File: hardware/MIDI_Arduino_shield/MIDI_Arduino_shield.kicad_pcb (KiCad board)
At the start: 2 copper layers, 54.6 x 69.8 mm, 31 parts, among them J2 MIDI OUT, J3 MIDI IN, J4 I2C, Q1 2N3906, SW1 RotaryEncoder_Switch, SW2 SW_Push, SW3 SW_Push, SW4 SW_DPDT_x2, U2 6N139

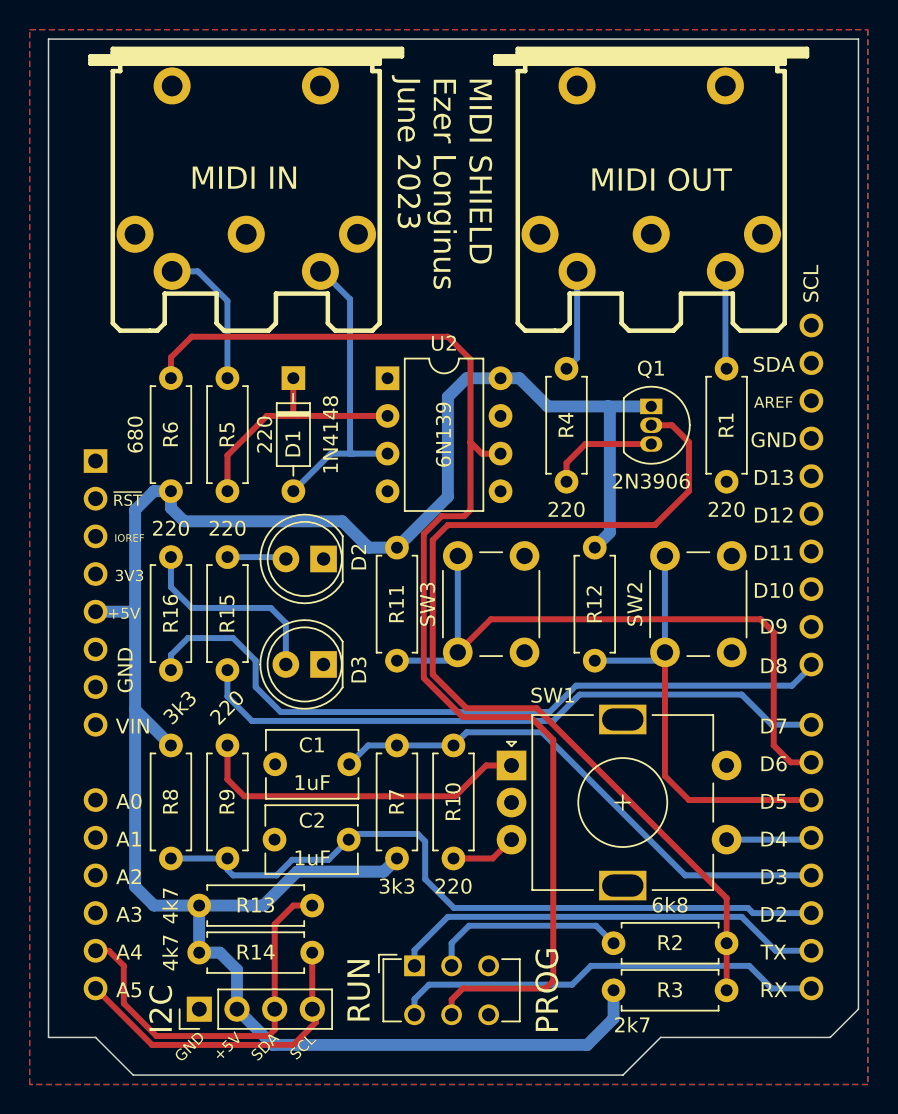
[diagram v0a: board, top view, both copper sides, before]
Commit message: MIDI Breakout Variations
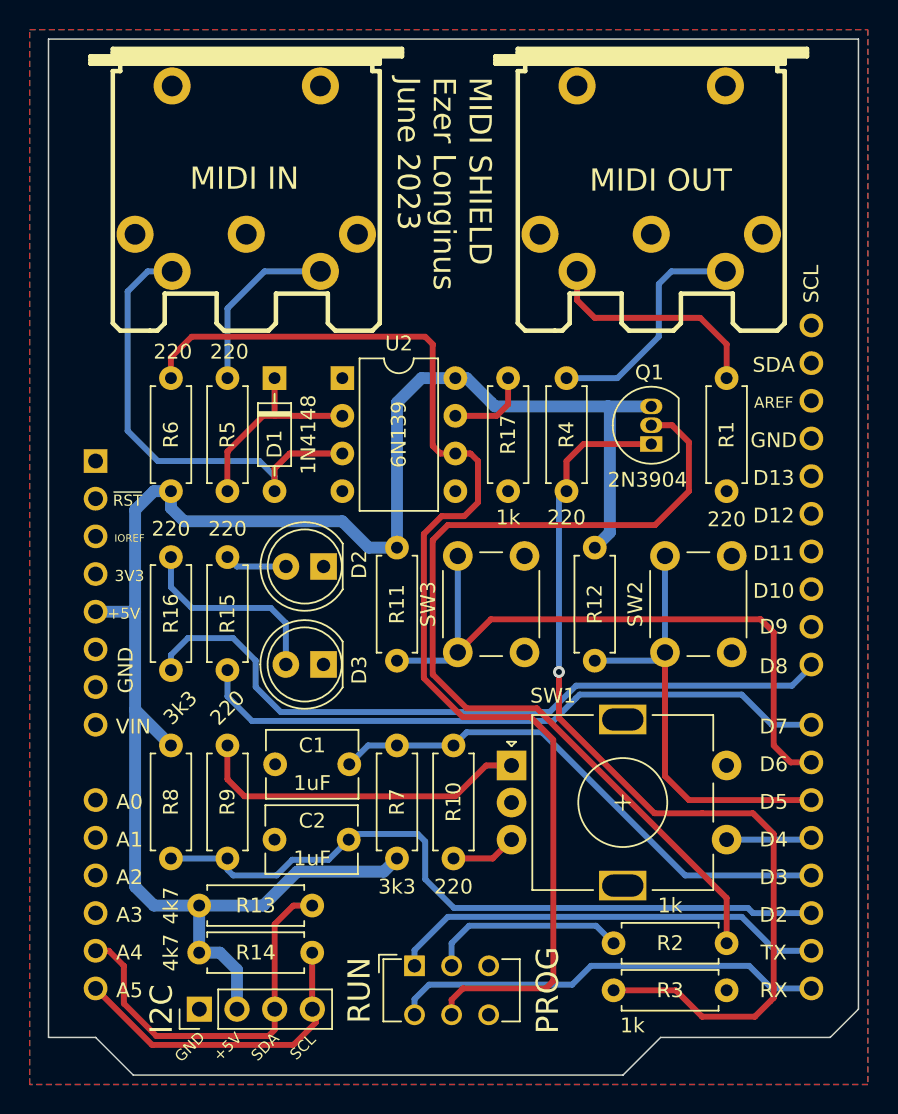
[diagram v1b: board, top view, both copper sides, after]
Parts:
- added R17: 1k, Resistor_THT:R_Axial_DIN0207_L6.3mm_D2.5mm_P7.62mm_Horizontal, F.Cu at (152.9, 78.7)
- Q1: value 2N3906 -> 2N3904
- R2: value 6k8 -> 1k
- R3: value 2k7 -> 1k
- R6: value 680 -> 220
- moved U2 3.05 mm to (141.7, 78.7)
- moved Q1 2.54 mm to (162.6, 83.2), turned to 90 degrees
- moved D1 1.27 mm to (137.2, 78.7)
- moved R4 0.64 mm to (156.8, 86.4)
- moved R1 0.63 mm to (167.6, 78.7)
- moved D2 0.51 mm to (140.5, 91.4)
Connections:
- J3 pad 4: Net-(J3-Pad4) -> Net-(D1-Pad2)
- J3 pad 5: Net-(D1-Pad2) -> Net-(J3-Pad5)
- Q1 pad 1: +5V -> Net-(Q1-Pad1)
- Q1 pad 3: Net-(Q1-Pad3) -> +5V
- R1 pad 1: Net-(J2-Pad5) -> Net-(J2-Pad4)
- R3 pad 1: +5V -> Net-(Q1-Pad1)
- R3 pad 2: Net-(Q1-Pad2) -> GND
- R4 pad 1: Net-(Q1-Pad3) -> Net-(Q1-Pad1)
- R4 pad 2: Net-(J2-Pad4) -> Net-(J2-Pad5)
- R5 pad 1: Net-(J3-Pad4) -> Net-(J3-Pad5)
- U2 pad 7: unconnected-(U2-Pad7) -> Net-(U2-Pad7)
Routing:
- net Net-(Q1-Pad1): track 0.00 -> 63.9 mm, vias 0 -> 1
- net +5V: track 145.9 -> 118.7 mm
- net Net-(J3-Pad5): track 0.00 -> 12.0 mm
- net Net-(D1-Pad2): track 20.6 -> 31.7 mm
- net Net-(J3-Pad4): track 9.76 -> 0.00 mm
- net Net-(J2-Pad5): track 6.60 -> 15.8 mm
- net Net-(J2-Pad4): track 6.86 -> 15.5 mm
- net Net-(Q1-Pad3): track 7.51 -> 0.00 mm
- net Net-(U2-Pad7): track 0.00 -> 5.65 mm
- net Net-(Q1-Pad2): track 66.3 -> 63.1 mm
- net Net-(D1-Pad1): track 17.0 -> 14.0 mm
- net Net-(R6-Pad1): track 83.9 -> 82.3 mm

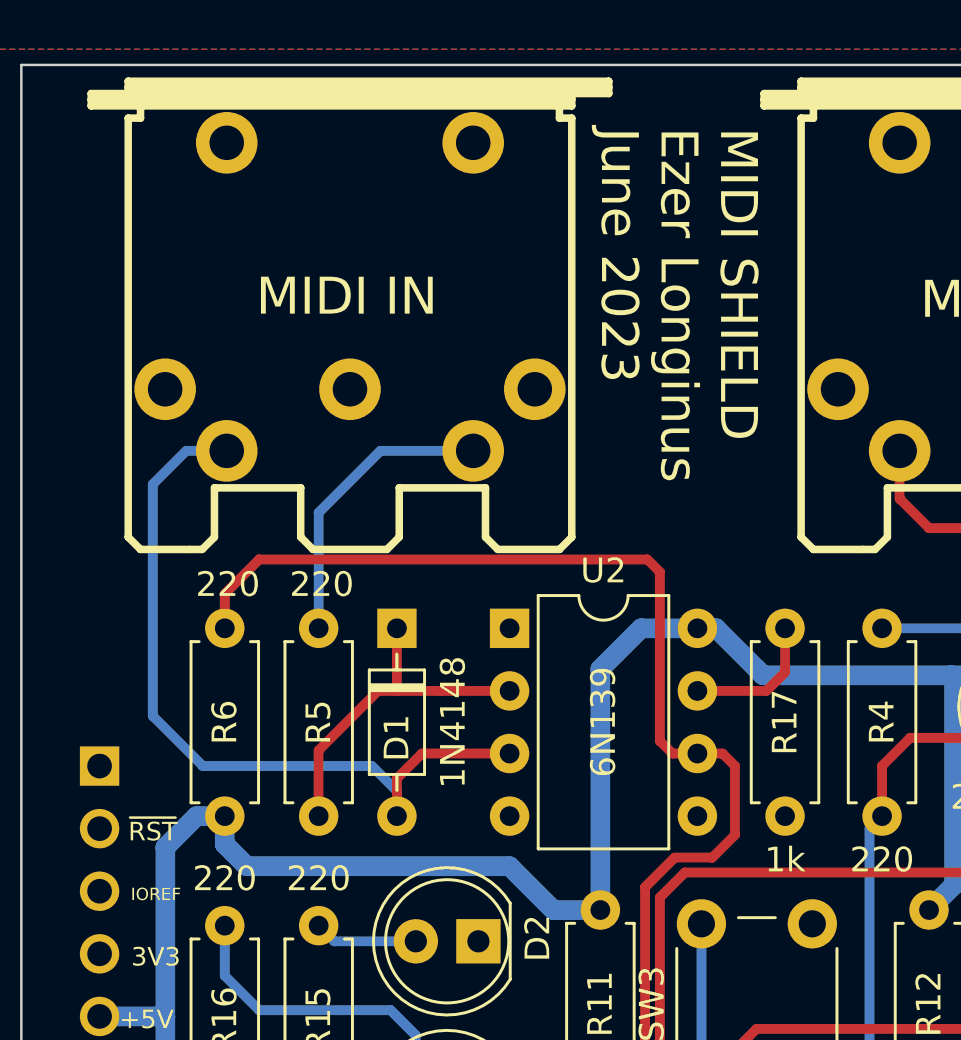
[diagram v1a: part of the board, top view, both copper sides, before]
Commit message: Fixed MIDI pinout swap
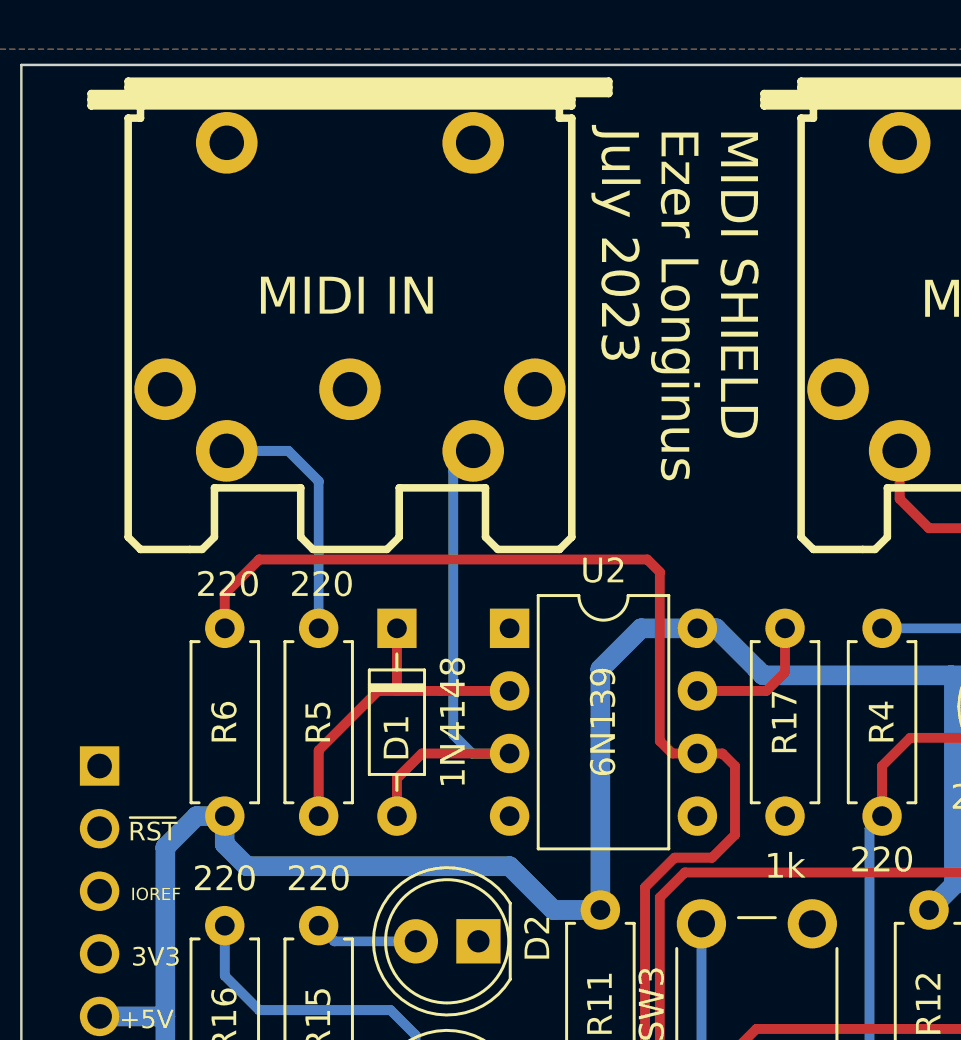
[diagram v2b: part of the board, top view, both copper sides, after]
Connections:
- J3 pad 4: Net-(D1-Pad2) -> Net-(J3-Pad4)
- J3 pad 5: Net-(J3-Pad5) -> Net-(D1-Pad2)
- R5 pad 1: Net-(J3-Pad5) -> Net-(J3-Pad4)
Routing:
- net Net-(J3-Pad5): track 12.0 -> 0.00 mm
- net Net-(D1-Pad2): track 31.7 -> 21.0 mm
- net Net-(J3-Pad4): track 0.00 -> 10.2 mm
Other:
- board text added: "MIDI SHIELD Ezer Longinus July 2023"
- board text removed: "MIDI SHIELD Ezer Longinus June 2023"
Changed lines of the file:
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@@
   (net 7 "unconnected-(J2-Pad1)")
   (net 8 "Net-(J2-Pad4)")
-  (net 9 "Net-(J3-Pad5)")
+  (net 9 "Net-(J3-Pad4)")
   (net 10 "Net-(Q1-Pad1)")
   (net 11 "Net-(D1-Pad1)")
@@
   (net 17 "unconnected-(U2-Pad1)")
   (net 18 "unconnected-(U2-Pad4)")
-  (net 19 "Net-(U2-Pad7)")
+  (net 19 "Net-(R17-Pad1)")
   (net 20 "D3")
   (net 21 "D2")
@@
     (fp_line (start 6.96 -1.25) (end 0.66 -1.25) (layer "F.Fab") (width 0.1))
     (pad "1" thru_hole circle (at 0 0 270) (size 1.6 1.6) (drill 0.8) (layers *.Cu *.Mask)
-      (net 9 "Net-(J3-Pad5)") (pintype "passive"))
+      (net 9 "Net-(J3-Pad4)") (pintype "passive"))
     (pad "2" thru_hole oval (at 7.62 0 270) (size 1.6 1.6) (drill 0.8) (layers *.Cu *.Mask)
       (net 11 "Net-(D1-Pad1)") (pintype "passive"))
@@
       (net 13 "unconnected-(J3-Pad3)") (pintype "passive"))
     (pad "4" thru_hole circle locked (at 5 -5.5 180) (size 2.5 2.5) (drill 1.4) (layers *.Cu *.Mask)
+      (net 9 "Net-(J3-Pad4)") (pintype "passive"))
+    (pad "5" thru_hole circle locked (at -5 -5.5 180) (size 2.5 2.5) (drill 1.4) (layers *.Cu *.Mask)
       (net 12 "Net-(D1-Pad2)") (pintype "passive"))
-    (pad "5" thru_hole circle locked (at -5 -5.5 180) (size 2.5 2.5) (drill 1.4) (layers *.Cu *.Mask)
-      (net 9 "Net-(J3-Pad5)") (pintype "passive"))
     (pad "6" thru_hole circle locked (at 5 7 180) (size 2.5 2.5) (drill 1.4) (layers *.Cu *.Mask))
     (pad "6" thru_hole circle locked (at -5 7 180) (size 2.5 2.5) (drill 1.4) (layers *.Cu *.Mask))
@@
       (effects (font (size 1 1) (thickness 0.15)))
     )
-    (fp_text value "1k" (at 9.398 0 180) (layer "F.SilkS")
+    (fp_text value "1k" (at 9.652 0 180) (layer "F.SilkS")
       (effects (font (size 1 1) (thickness 0.15)))
     )
@@
     (fp_line (start 6.96 -1.25) (end 0.66 -1.25) (layer "F.Fab") (width 0.1))
     (pad "1" thru_hole circle (at 0 0 270) (size 1.6 1.6) (drill 0.8) (layers *.Cu *.Mask)
-      (net 19 "Net-(U2-Pad7)") (pintype "passive"))
+      (net 19 "Net-(R17-Pad1)") (pintype "passive"))
     (pad "2" thru_hole oval (at 7.62 0 270) (size 1.6 1.6) (drill 0.8) (layers *.Cu *.Mask)
       (net 1 "GND") (pintype "passive"))
@@
       (net 47 "Net-(R6-Pad1)") (pinfunction "VO2") (pintype "passive"))
     (pad "7" thru_hole oval (at 7.62 2.54) (size 1.6 1.6) (drill 0.8) (layers *.Cu *.Mask)
-      (net 19 "Net-(U2-Pad7)") (pinfunction "VO1") (pintype "passive"))
+      (net 19 "Net-(R17-Pad1)") (pinfunction "VO1") (pintype "passive"))
     (pad "8" thru_hole oval (at 7.62 0) (size 1.6 1.6) (drill 0.8) (layers *.Cu *.Mask)
       (net 2 "+5V") (pinfunction "VCC") (pintype "passive"))
@@
     (effects (font (size 1 1) (thickness 0.15)))
   )
-  (gr_text "MIDI SHIELD\nEzer Longinus\nJune 2023" (at 148.59 58.42 270) (layer "F.SilkS")
+  (gr_text "MIDI SHIELD\nEzer Longinus\nJuly 2023" (at 148.59 58.42 270) (layer "F.SilkS")
     (effects (font (size 1.5 1.5) (thickness 0.2)) (justify left))
   )
@@
   (segment (start 167.64 78.74) (end 167.64 76.454) (width 0.4) (layer "F.Cu") (net 8))
   (segment (start 157.56 73.486) (end 157.56 71.54) (width 0.4) (layer "F.Cu") (net 8))
-  (segment (start 133.985 78.74) (end 133.985 74.041) (width 0.4) (layer "B.Cu") (net 9))
-  (segment (start 136.486 71.54) (end 140.255 71.54) (width 0.4) (layer "B.Cu") (net 9))
-  (segment (start 133.985 74.041) (end 136.486 71.54) (width 0.4) (layer "B.Cu") (net 9))
+  (segment (start 132.754 71.54) (end 133.985 72.771) (width 0.4) (layer "B.Cu") (net 9))
+  (segment (start 133.985 72.771) (end 133.985 78.74) (width 0.4) (layer "B.Cu") (net 9))
+  (segment (start 130.255 71.54) (end 132.754 71.54) (width 0.4) (layer "B.Cu") (net 9))
   (segment (start 165.989 108.077) (end 162.773528 108.077) (width 0.4) (layer "F.Cu") (net 10))
   (segment (start 164.211 120.015) (end 165.989 121.793) (width 0.4) (layer "F.Cu") (net 10))
@@
   (segment (start 138.176 83.82) (end 137.16 84.836) (width 0.4) (layer "F.Cu") (net 12))
   (segment (start 141.732 83.82) (end 138.176 83.82) (width 0.4) (layer "F.Cu") (net 12))
-  (segment (start 136.144 84.328) (end 137.16 85.344) (width 0.4) (layer "B.Cu") (net 12))
-  (segment (start 128.612 71.54) (end 127.254 72.898) (width 0.4) (layer "B.Cu") (net 12))
-  (segment (start 137.16 85.344) (end 137.16 86.36) (width 0.4) (layer "B.Cu") (net 12))
-  (segment (start 127.254 72.898) (end 127.254 82.296) (width 0.4) (layer "B.Cu") (net 12))
-  (segment (start 129.286 84.328) (end 136.144 84.328) (width 0.4) (layer "B.Cu") (net 12))
-  (segment (start 130.255 71.54) (end 128.612 71.54) (width 0.4) (layer "B.Cu") (net 12))
-  (segment (start 127.254 82.296) (end 129.286 84.328) (width 0.4) (layer "B.Cu") (net 12))
+  (segment (start 140.208 83.82) (end 139.446 83.058) (width 0.4) (layer "B.Cu") (net 12))
+  (segment (start 139.446 83.058) (end 139.446 72.349) (width 0.4) (layer "B.Cu") (net 12))
+  (segment (start 139.446 72.349) (end 140.255 71.54) (width 0.4) (layer "B.Cu") (net 12))
+  (segment (start 141.732 83.82) (end 140.208 83.82) (width 0.4) (layer "B.Cu") (net 12))
   (segment (start 162.814 88.646) (end 148.844 88.646) (width 0.4) (layer "F.Cu") (net 14))
   (segment (start 162.56 81.915) (end 163.957 81.915) (width 0.4) (layer "F.Cu") (net 14))
